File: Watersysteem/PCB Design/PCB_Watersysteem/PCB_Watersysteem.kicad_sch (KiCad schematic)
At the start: 56 parts, among them J1 Screw_Terminal_01x02, J10 LED Water Level, J11 LED Nutrient Level, J12 Height Nutrients, J13 Height Mixer, J2 Conn_01x04_Pin, J21 Voedingstoffen 1, J3 ReferentieProbe, J4 Voedingstoffen 2, J5 Voedingstoffen 3, J6 Height Water, J7 Endstop Water, J8 Endstop Nutrients, J9 Endstop Mixer, SW1 EN, SW2 BOOT, U1 ESP32-WROOM-32D, U2 MP1584_Module, U3 AMS1117-3.3, U4 ADS1115IDGS

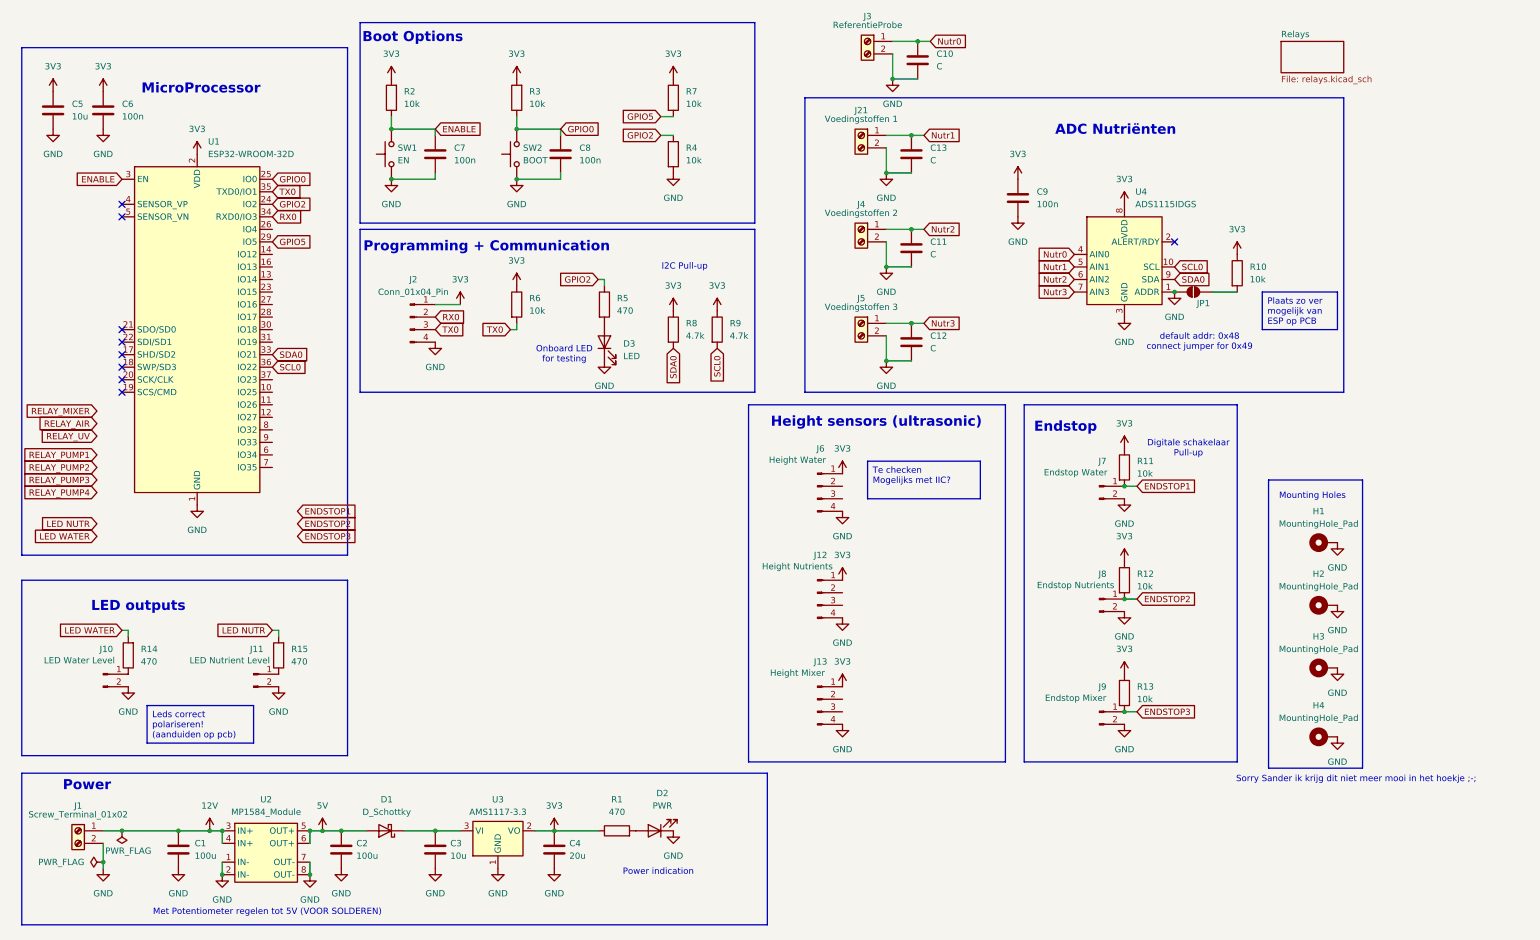
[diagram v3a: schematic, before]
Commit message: Update PCB
relaisschakelingen verder afgewerkt, endstops afgewerkt, bezig met ultrasone sensors
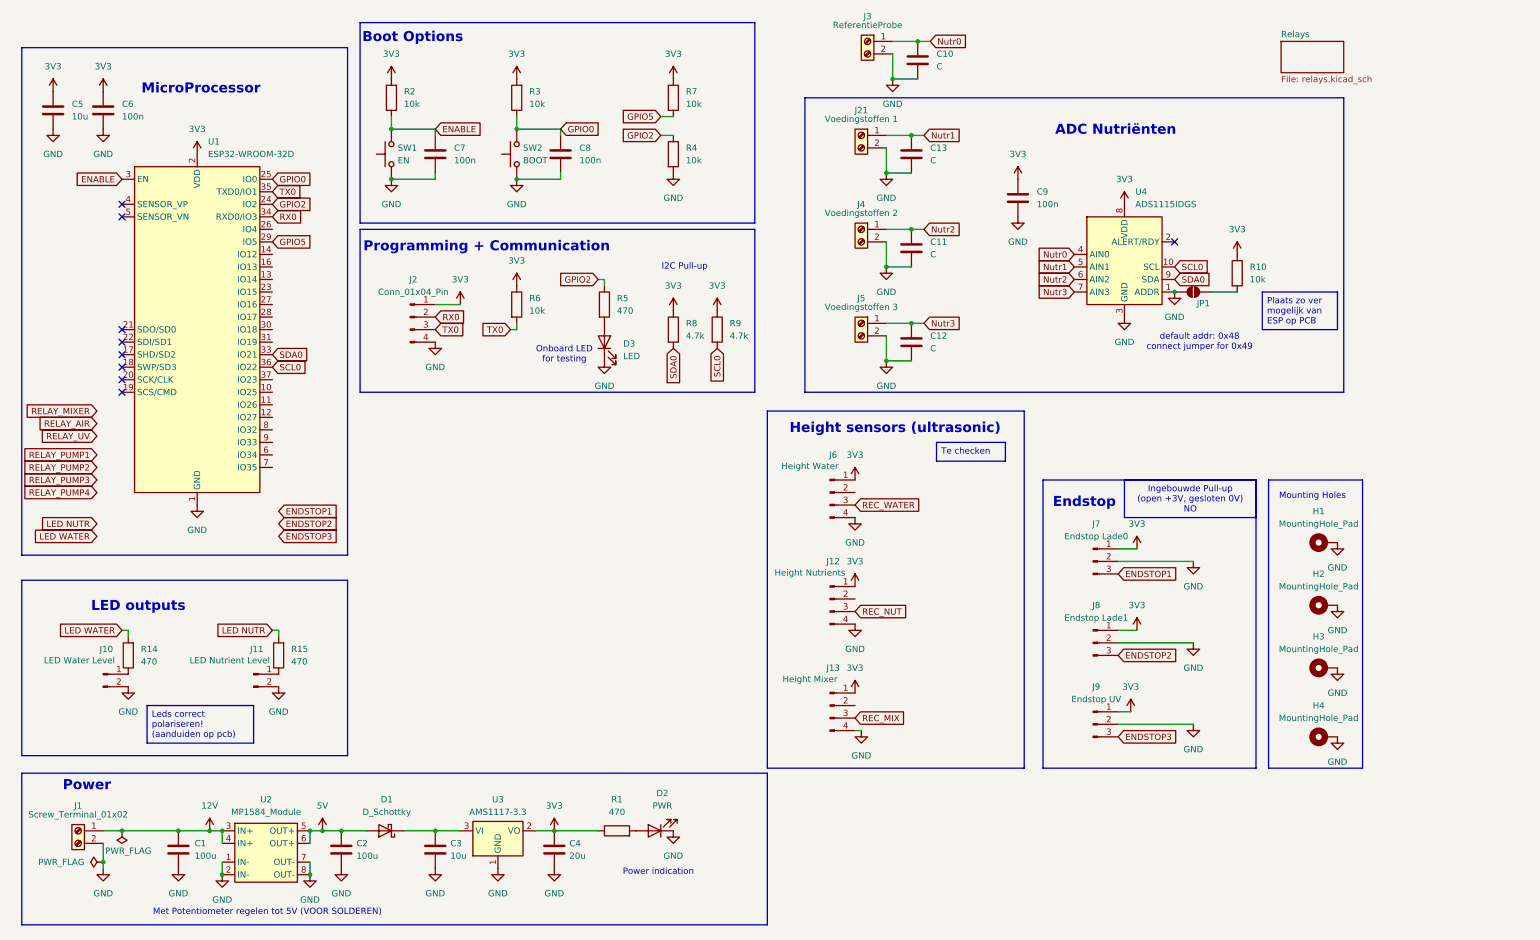
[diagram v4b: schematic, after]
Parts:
- removed J7: Endstop Water, symbol Connector:Conn_01x02_Pin
- removed J8: Endstop Nutrients, symbol Connector:Conn_01x02_Pin
- removed J9: Endstop Mixer, symbol Connector:Conn_01x02_Pin
- removed R11, R12, R13: 10k, symbol Device:R
- added J7: Endstop Lade0, symbol Connector:Conn_01x03_Pin
- added J8: Endstop Lade1, symbol Connector:Conn_01x03_Pin
- added J9: Endstop UV, symbol Connector:Conn_01x03_Pin
- H1, H2, H3, H4, JP1: now in the parts list
- U2: footprint (none) -> Watersysteem_Footprints_Library:MP1584_Module
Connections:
- net 3V3: now also J7.1 (Pin_1), J8.1 (Pin_1), J9.1 (Pin_1)
- net ENDSTOP1: now also J7.3 (Pin_3)
- net ENDSTOP2: now also J8.3 (Pin_3)
- net ENDSTOP3: now also J9.3 (Pin_3)
- net GND: now also J7.2 (Pin_2), J8.2 (Pin_2), J9.2 (Pin_2)
- net REC_NUT: now reaches J12.3 (Pin_3)
- net REC_MIX: now reaches J13.3 (Pin_3)
- net REC_WATER: now reaches J6.3 (Pin_3)
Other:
- note removed: "Digitale schakelaar Pull-up"
- note removed: "Sorry Sander ik krijg dit niet meer mooi in het hoekje ;-;"
- moved on the sheet: J12, J13, J6

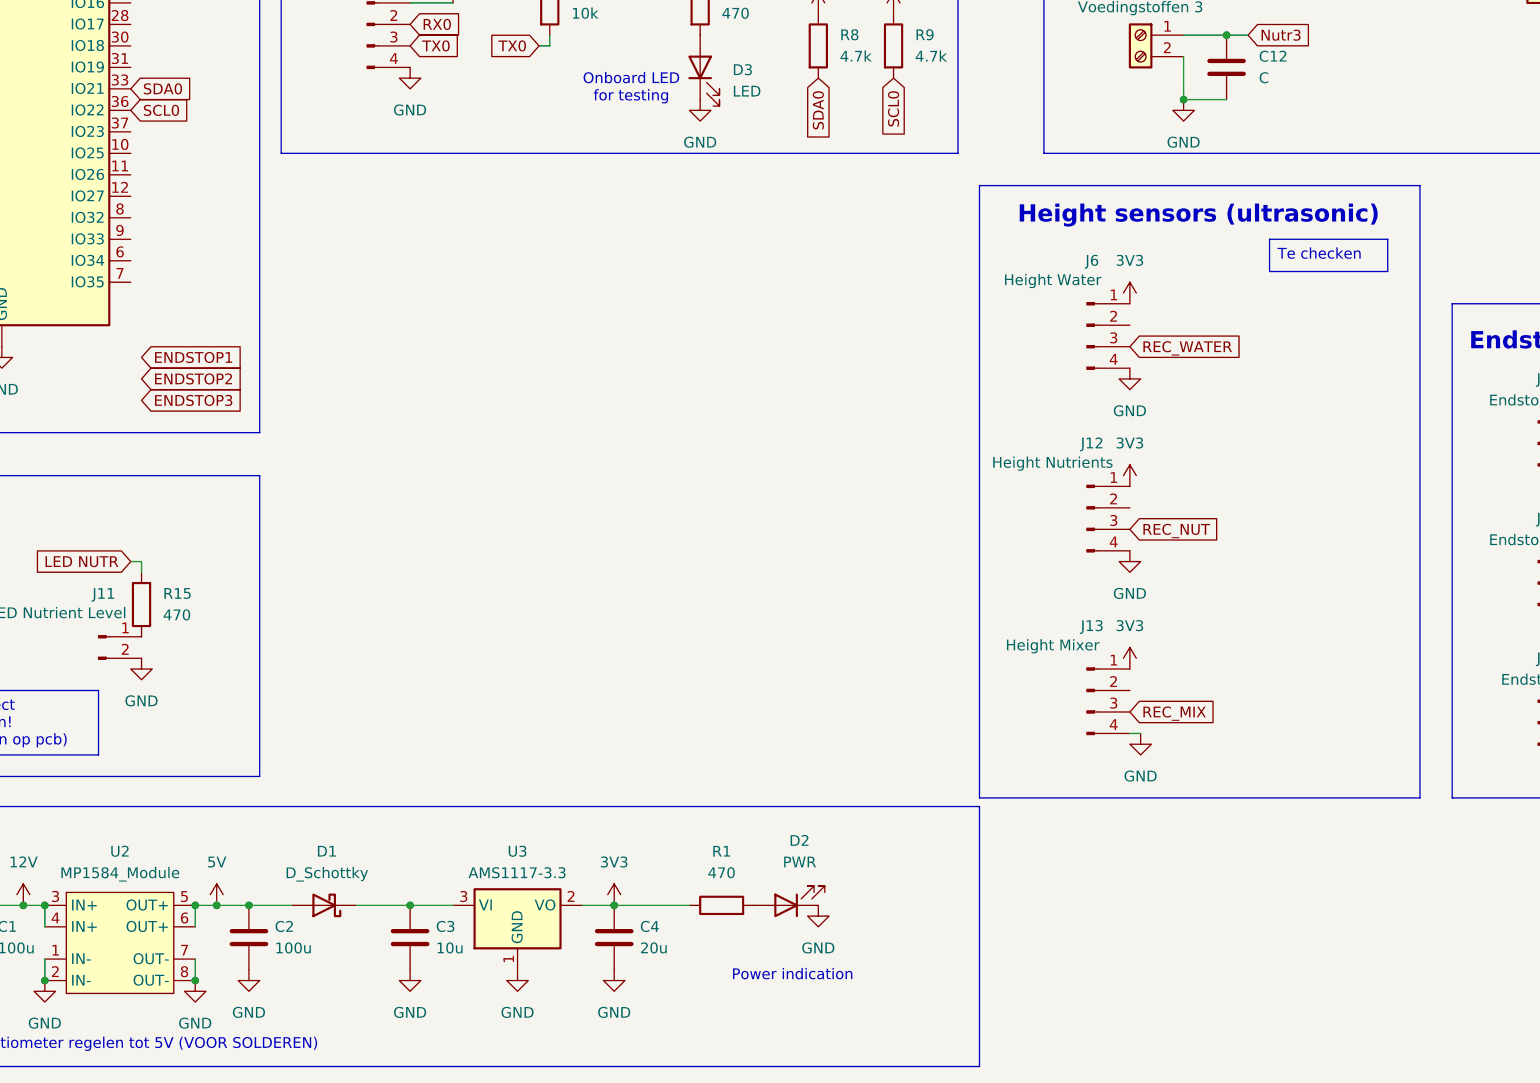
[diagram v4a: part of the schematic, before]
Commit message: Update PCB
deel footprints geselecteerd, hoogtesensoren ingesteld
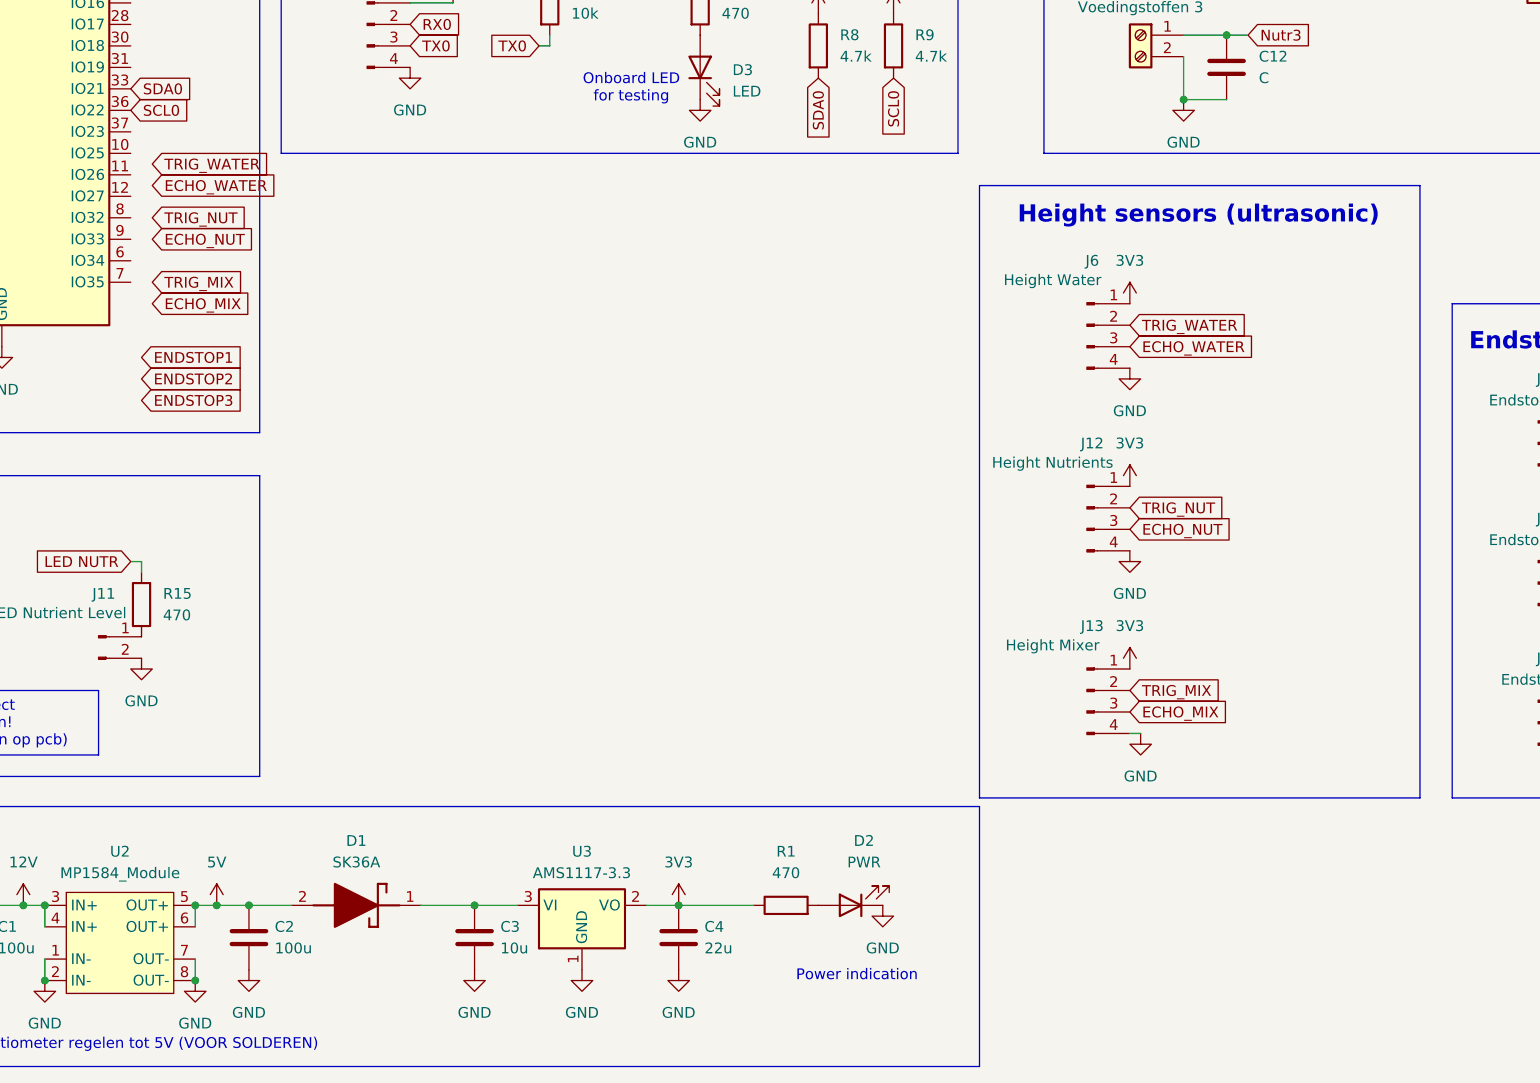
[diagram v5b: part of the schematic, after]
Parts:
- removed D1: D_Schottky, symbol Device:D_Schottky
- added D1: SK36A, SamacSys_Parts:DIOM5226X290N, symbol SamacSys_Parts:SK36A
- C3, C5, C6, C7, C8, C9: footprint (none) -> Capacitor_SMD:C_0805_2012Metric_Pad1.18x1.45mm_HandSolder
- C4: value 20u -> 22u
- R1, R10, R14, R15, R2, R3, R4, R5, R6, R7, R8, R9: footprint (none) -> Resistor_SMD:R_0805_2012Metric_Pad1.20x1.40mm_HandSolder
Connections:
- net 5V: now also D1.2 (A)
- net at C3.1, U3.3 (VI): now also D1.1 (K)
- net TRIG_NUT: now reaches J12.2 (Pin_2)
- net TRIG_MIX: now reaches J13.2 (Pin_2)
- net TRIG_WATER: now reaches J6.2 (Pin_2)
- net REC_MIX renamed ECHO_MIX
- net REC_NUT renamed ECHO_NUT
- net REC_WATER renamed ECHO_WATER
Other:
- moved on the sheet: C3, C4, D2, R1, U3

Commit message: Update PCB
Footprints LEDs toegevoegd
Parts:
- D2, D3: footprint (none) -> LED_SMD:LED_0805_2012Metric_Pad1.15x1.40mm_HandSolder
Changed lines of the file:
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@@
 			)
 		)
-		(property "Footprint" ""
+		(property "Footprint" "LED_SMD:LED_0805_2012Metric_Pad1.15x1.40mm_HandSolder"
 			(at 148.59 177.8 0)
 			(effects
@@
 			)
 		)
-		(property "Footprint" ""
+		(property "Footprint" "LED_SMD:LED_0805_2012Metric_Pad1.15x1.40mm_HandSolder"
 			(at 130.81 78.74 0)
 			(effects

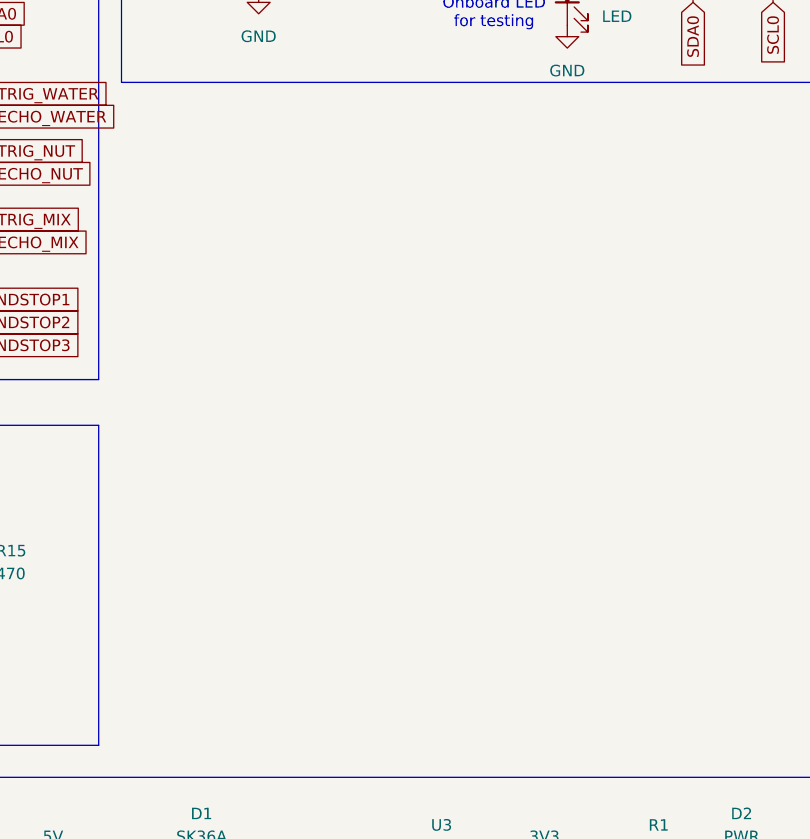
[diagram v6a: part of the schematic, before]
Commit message: Update PCB
16 bit I2C IO expander toegevoegd (juiste footprint nog na te meten)
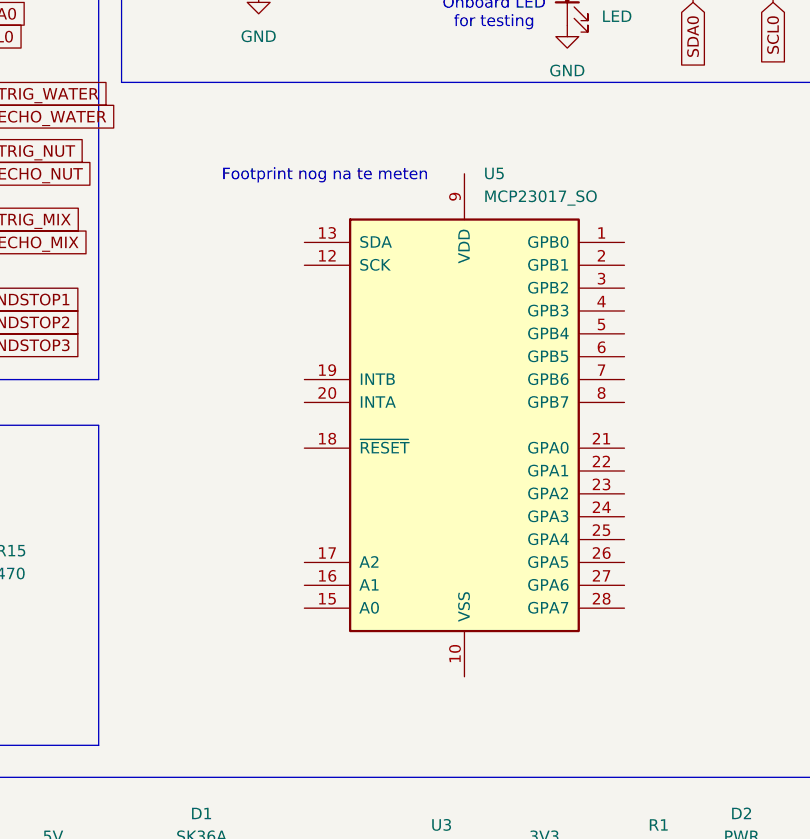
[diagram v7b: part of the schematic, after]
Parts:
- added U5: MCP23017_SO, Package_SO:SOIC-28W_7.5x17.9mm_P1.27mm, symbol Interface_Expansion:MCP23017_SO
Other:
- note added: "Footprint nog na te meten"
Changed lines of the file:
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@@
 		)
 	)
+	(text "Footprint nog na te meten"
+		(exclude_from_sim no)
+		(at 103.886 99.314 0)
+		(effects
+			(font
+				(size 1.27 1.27)
+			)
+		)
+	)
 	(text "Onboard LED\nfor testing"
 		(exclude_from_sim no)
@@
 					(unit 1)
 				)
+			)
+		)
+	)
+	(symbol
+		(lib_id "Interface_Expansion:MCP23017_SO")
+		(at 119.38 127 0)
+		(unit 1)
+		(exclude_from_sim no)
+		(in_bom yes)
+		(on_board yes)
+		(dnp no)
+		(fields_autoplaced yes)
+		(property "Reference" "U5"
+			(at 121.5233 99.06 0)
+			(effects
+				(font
+					(size 1.27 1.27)
+				)
+				(justify left)
+			)
+		)
+		(property "Value" "MCP23017_SO"
+			(at 121.5233 101.6 0)
+			(effects
+				(font
+					(size 1.27 1.27)
+				)
+				(justify left)
+			)
+		)
+		(property "Footprint" "Package_SO:SOIC-28W_7.5x17.9mm_P1.27mm"
+			(at 124.46 152.4 0)
+			(effects
+				(font
+					(size 1.27 1.27)
+				)
+				(justify left)
+				(hide yes)
+			)
+		)
+		(property "Datasheet" "https://ww1.microchip.com/downloads/aemDocuments/documents/APID/ProductDocuments/DataSheets/MCP23017-Data-Sheet-DS20001952.pdf"
+			(at 124.46 154.94 0)
+			(effects
+				(font
+					(size 1.27 1.27)
+				)
+				(justify left)
+				(hide yes)
+			)
+		)
+		(property "Description" "16-bit I/O expander, I2C, interrupts, w pull-ups, GPA/B7 output only (https://microchip.my.site.com/s/article/GPA7---GPB7-Cannot-Be-Used-as-Inputs-In-MCP23017),  SOIC-28"
+			(at 119.38 127 0)
+			(effects
+				(font
+					(size 1.27 1.27)
+				)
+				(hide yes)
+			)
+		)
+		(pin "21"
+		)
+		(pin "25"
+		)
+		(pin "5"
+		)
+		(pin "15"
+		)
+		(pin "17"
+		)
+		(pin "10"
+		)
+		(pin "2"
+		)
+		(pin "13"
+		)
+		(pin "23"
+		)
+		(pin "24"
+		)
+		(pin "12"
+		)
+		(pin "20"
+		)
+		(pin "4"
+		)
+		(pin "9"
+		)
+		(pin "6"
+		)
+		(pin "7"
+		)
+		(pin "18"
+		)
+		(pin "1"
+		)
+		(pin "16"
+		)
+		(pin "14"
+		)
+		(pin "19"
+		)
+		(pin "3"
+		)
+		(pin "8"
+		)
+		(pin "11"
+		)
+		(pin "22"
+		)
+		(pin "28"
+		)
+		(pin "26"
+		)
+		(pin "27"
+		)
+		(instances
+			(project ""
+				(path "/de0b8b90-8fde-4ab1-b1b1-e85d44454ecd"
+					(reference "U5")
+					(unit 1)
+				)
